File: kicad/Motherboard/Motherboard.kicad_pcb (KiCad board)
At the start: 2 copper layers, 57.3 x 62.8 mm, 72 parts, among them J1 USB_C_Receptacle_USB2.0, J10 Conn_01x08_Pin, J11 Conn_01x08_Pin, J12 Conn_01x08_Pin, J13 Conn_01x08_Pin, J2 Conn_01x02_Pin, J3 Conn_01x04_Pin, J4 Conn_01x04_Pin, J5 Conn_01x02_Pin, J6 Conn_01x08_Pin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

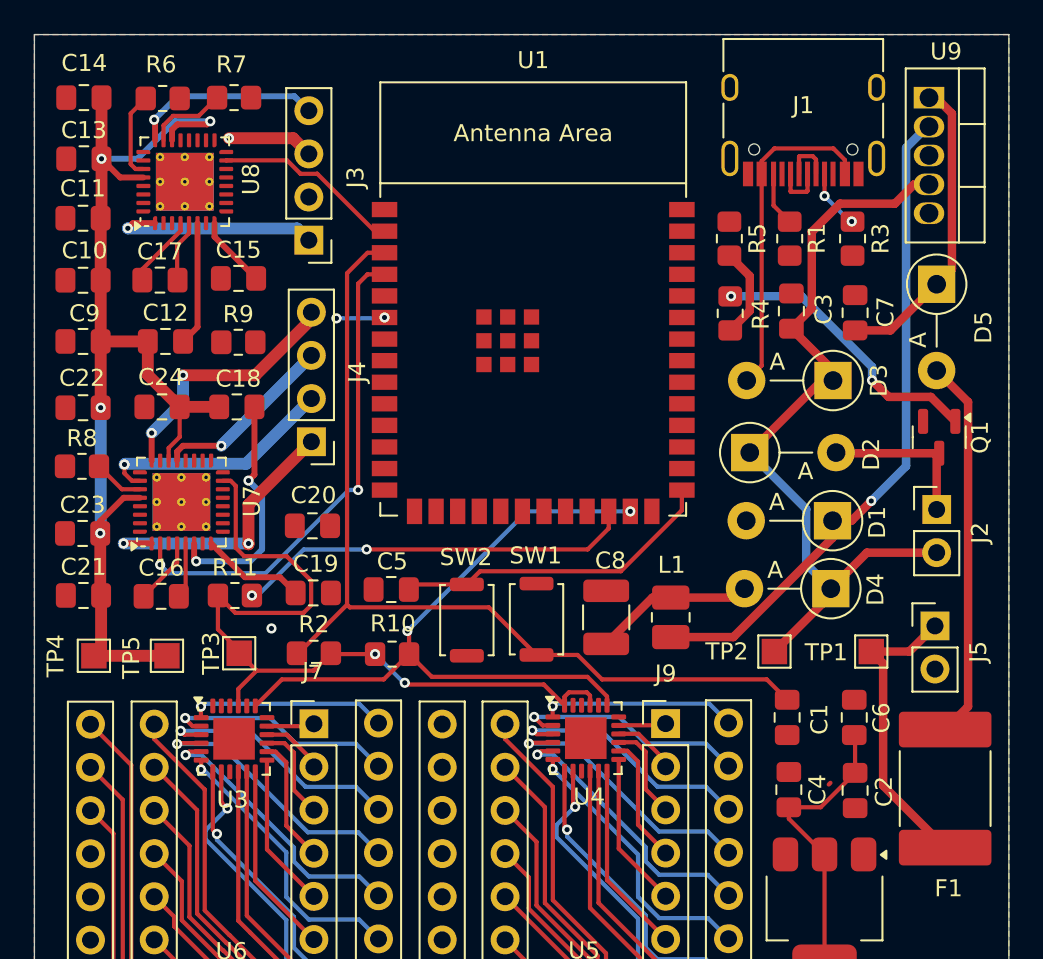
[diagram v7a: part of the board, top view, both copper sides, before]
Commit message: I think we need to change something about the motor controllers
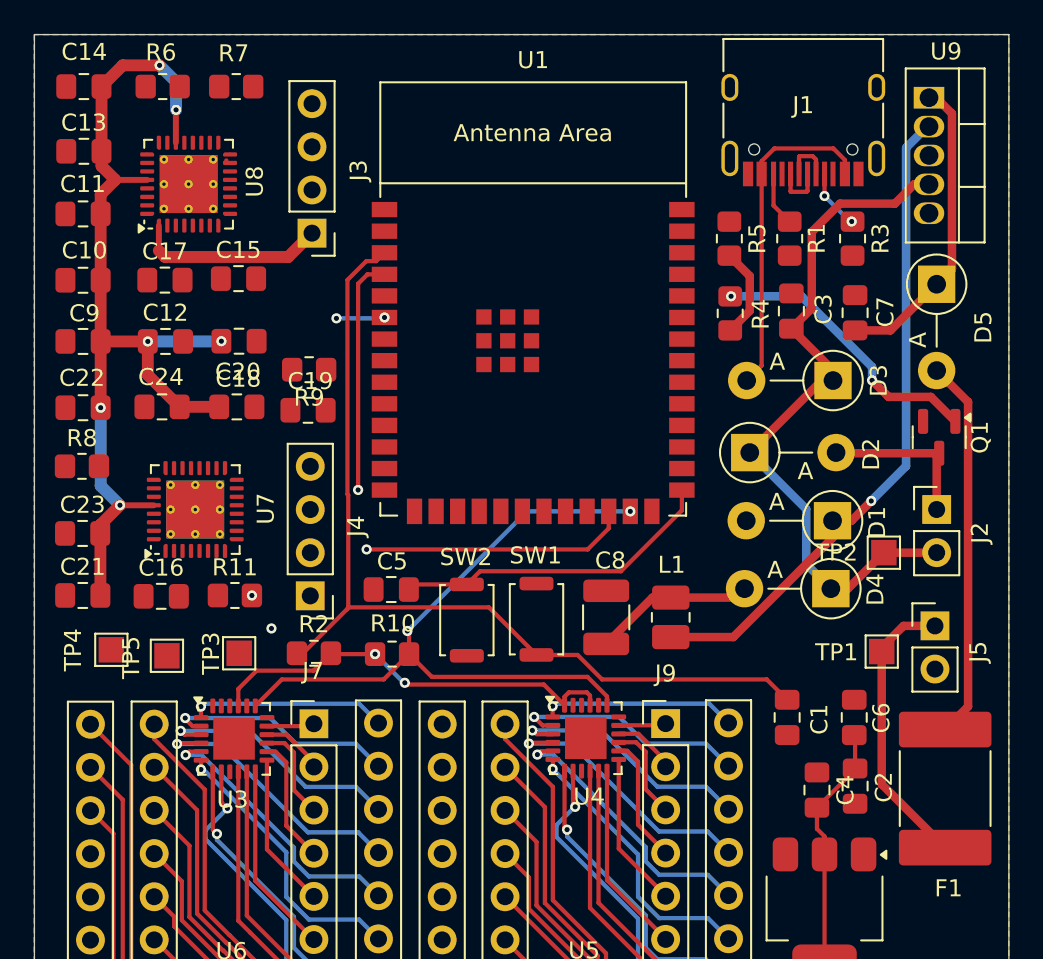
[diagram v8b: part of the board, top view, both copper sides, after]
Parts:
- moved C20 11.7 mm to (128.3, 75.9), turned to 0 degrees
- moved C19 10.8 mm to (132.4, 80.0)
- moved J4 9.07 mm to (132.5, 90.9)
- moved TP2 8.68 mm to (166.2, 88.4)
- moved R9 4.47 mm to (132.4, 77.6), turned to 180 degrees
- moved C4 1.66 mm to (162.3, 102.4)
- moved TP4 1.09 mm to (120.8, 94.1)
- moved U7 0.93 mm to (125.7, 85.9)
- moved R6 0.70 mm to (123.8, 61.0)
- moved R7 0.66 mm to (128.1, 61.0)
- moved C14 0.65 mm to (119.2, 61.0)
- moved TP1 0.62 mm to (166.1, 94.2)
- moved J3 0.45 mm to (132.6, 69.6)
- moved C13 0.44 mm to (119.2, 64.8)
- moved C17 0.29 mm to (123.9, 72.3)
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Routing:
- net +3.3V: track 75.8 -> 40.4 mm
- net Motor4_2: track 16.6 -> 0.00 mm, vias 2 -> 0
- net ENN_2: track 29.1 -> 13.9 mm, vias 2 -> 1
- net Motor1_2: track 15.1 -> 0.00 mm, vias 2 -> 0
- net Motor3_2: track 14.2 -> 0.00 mm, vias 1 -> 0
- net VCP_2: track 14.1 -> 0.00 mm, vias 2 -> 0
- net Motor1_1: track 11.3 -> 0.37 mm, vias 1 -> 0
- net Motor2_2: track 10.8 -> 0.00 mm, vias 1 -> 0
- net VS_1: track 85.5 -> 76.6 mm, vias 4 -> 6
- net SDA: track 23.6 -> 16.1 mm
- net VCP_1: track 7.31 -> 0.00 mm
- net 5VOUT_2: track 6.18 -> 0.00 mm
- net Net-(U8-BRB): track 5.10 -> 0.00 mm
- net Motor2_1: track 5.08 -> 0.00 mm, vias 1 -> 0
- net Net-(U8-BRA): track 4.71 -> 0.00 mm
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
